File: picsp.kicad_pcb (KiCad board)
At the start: 2 copper layers, 56.9 x 24.6 mm, 3 parts, among them J1 Raspberry_Pi_2_3, J2 ICSP10, J3 ICSP6

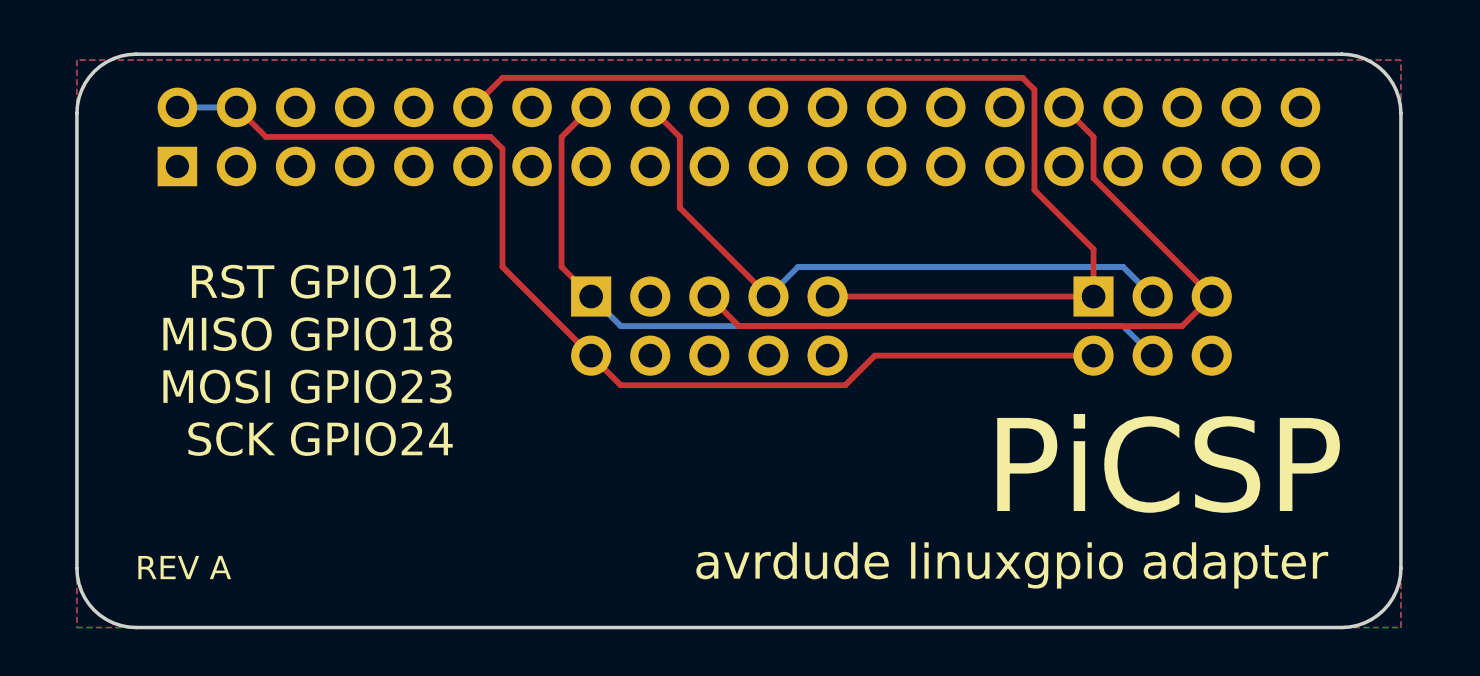
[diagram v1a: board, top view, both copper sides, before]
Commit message: Nudge the PCB slightly to align to 1.27mm grid
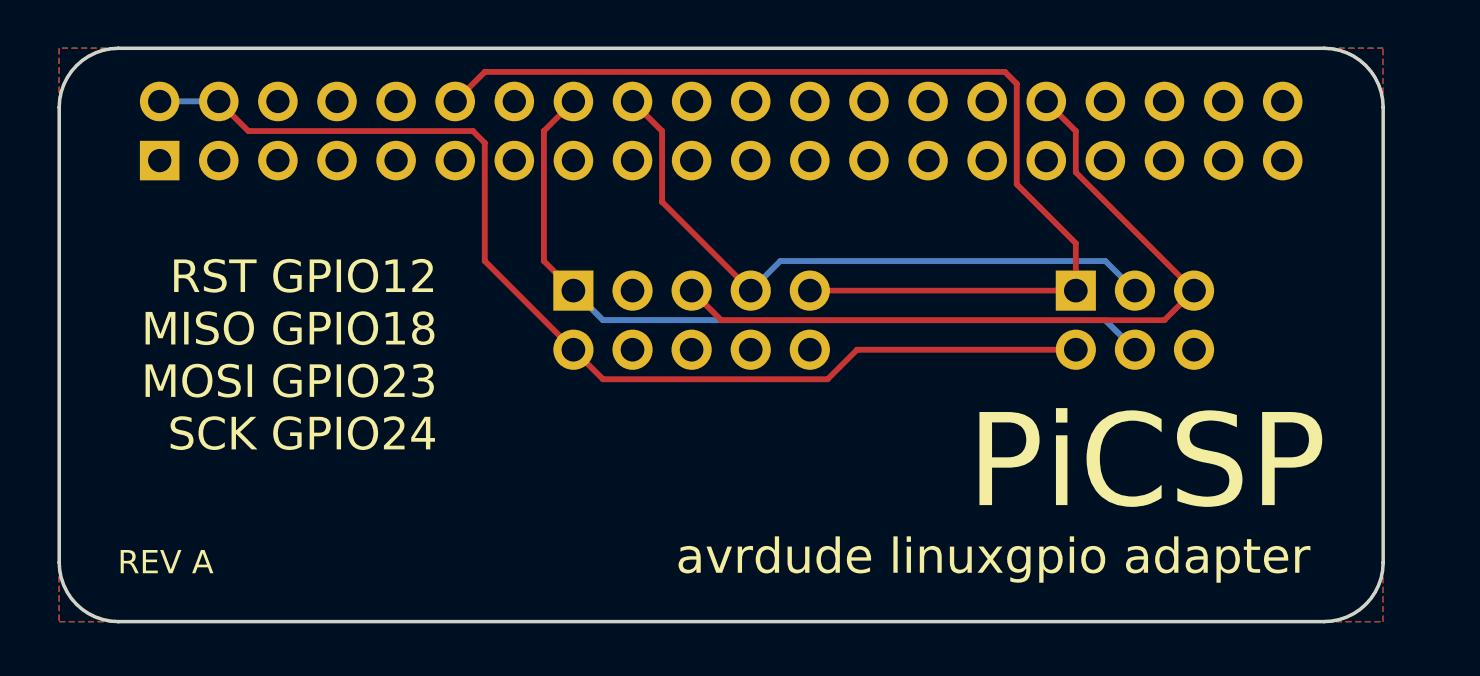
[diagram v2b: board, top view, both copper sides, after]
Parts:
- moved J2 0.80 mm to (137.2, 103.4)
- moved J3 0.80 mm to (158.8, 103.4)
- moved J1 0.80 mm to (119.4, 97.8)

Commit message: Update project to 5.0 RC1
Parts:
- J1: footprint Socket_Strips:Socket_Strip_Straight_2x20_Pitch2.54mm -> Connector_PinSocket_2.54mm:PinSocket_2x20_P2.54mm_Vertical
- J2: footprint Connectors_IDC:IDC-Header_2x05_Pitch2.54mm_Angled -> Connector_IDC:IDC-Header_2x05_P2.54mm_Horizontal
- J3: footprint Connectors_IDC:IDC-Header_2x03_Pitch2.54mm_Angled -> Connector_IDC:IDC-Header_2x03_P2.54mm_Horizontal

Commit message: Update to use new library symbols
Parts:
- J2: value ICSP10 -> AVR-ISP-10
- J3: value ICSP6 -> AVR-ISP-6
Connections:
- net MISO renamed /MISO
- net MOSI renamed /MOSI
- net RST renamed /RST
- net SCK renamed /SCK
